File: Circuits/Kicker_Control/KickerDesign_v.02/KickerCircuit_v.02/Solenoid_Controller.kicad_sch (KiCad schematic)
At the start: 7 parts, among them Q2 NMOS, U4 VS-5EWH06FN-M3

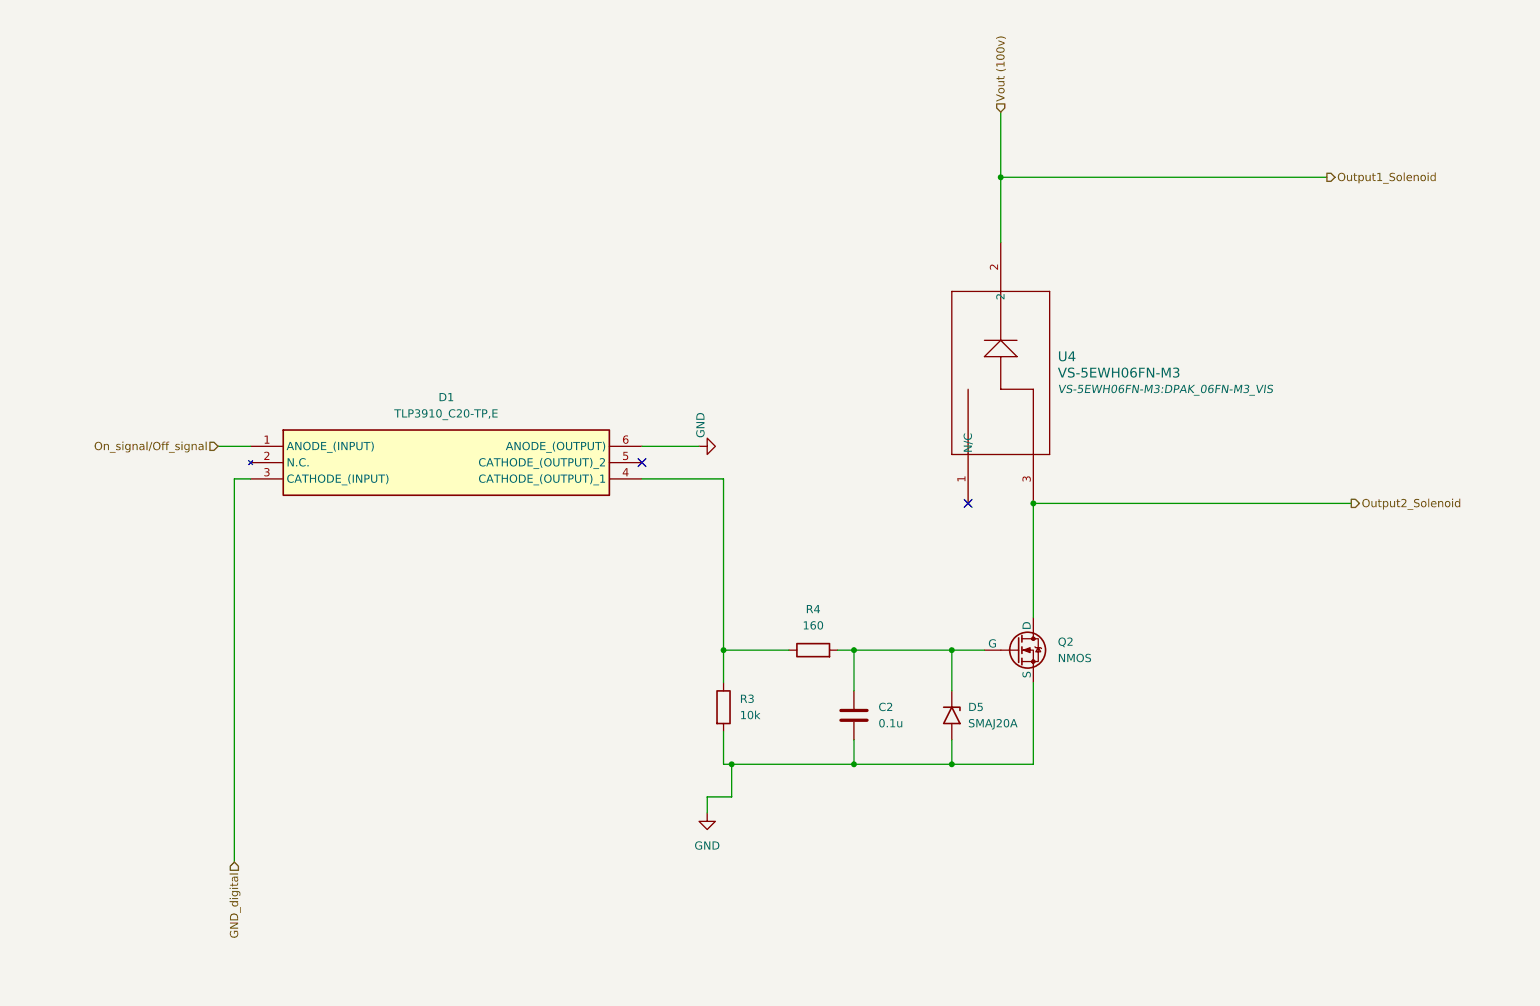
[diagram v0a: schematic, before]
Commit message: Changes in the kicker circuit
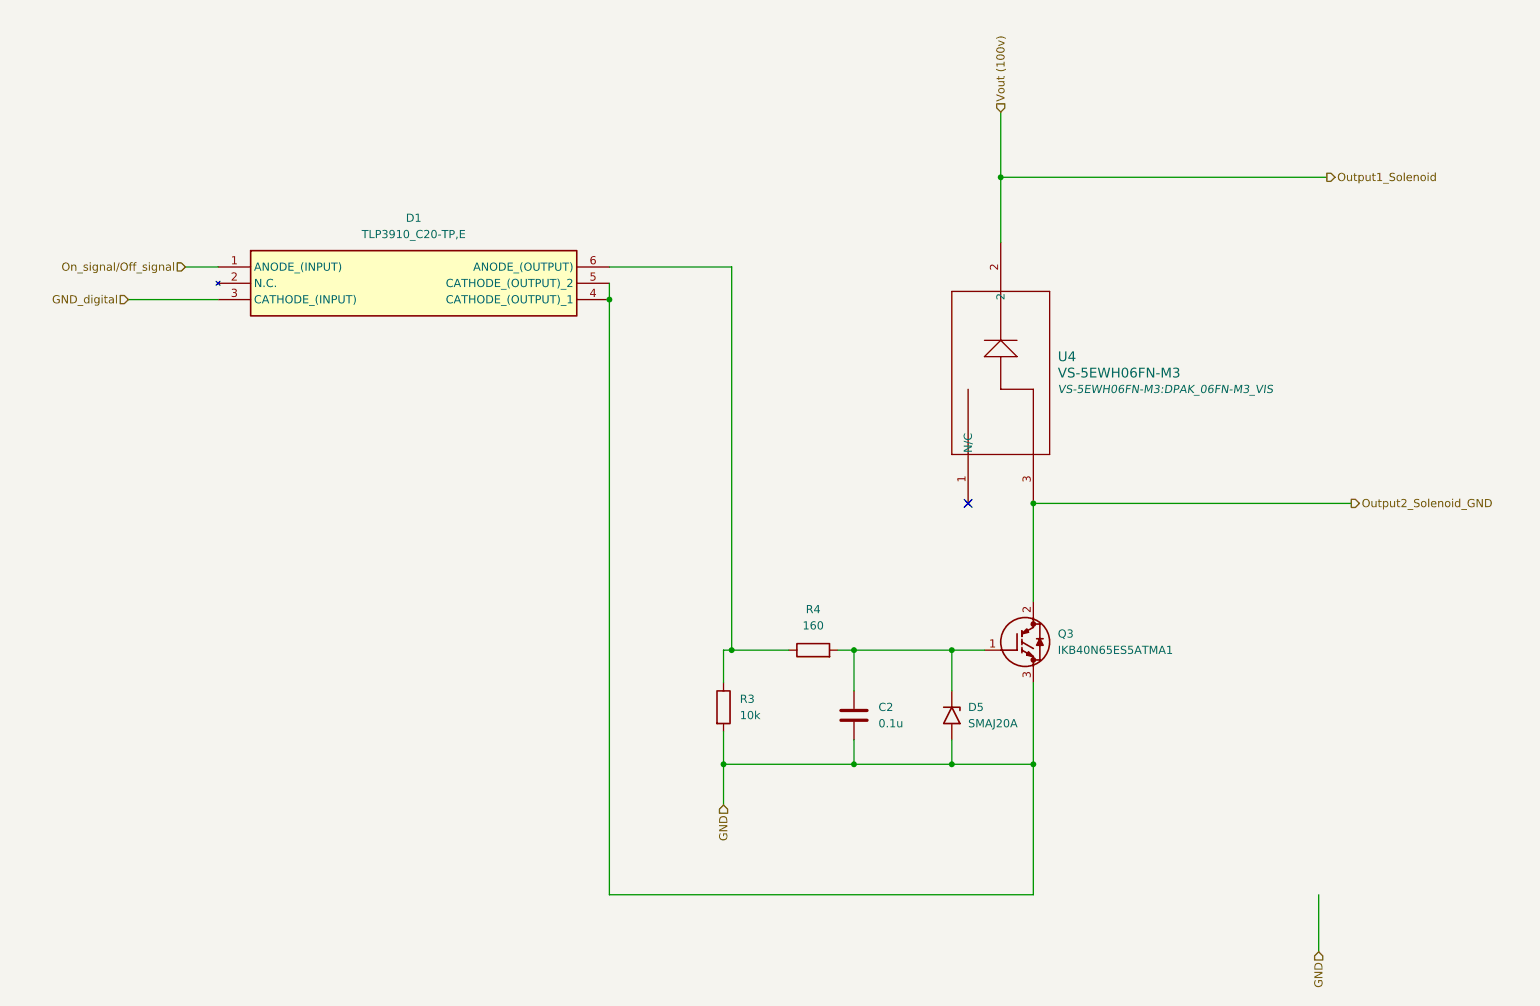
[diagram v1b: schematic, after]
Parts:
- removed Q2: NMOS, symbol Simulation_SPICE:NMOS
- added Q3: IKB40N65ES5ATMA1, BTS141TCBUMA1, symbol IKB40N65ES5ATMA1:IKB40N65ES5ATMA1
- D1: footprint SOIC127P1000X220-6N -> TLP3910_C20-TP,E:SOIC127P1000X220-6N
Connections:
- net GND: now also D1.4 (CATHODE_(OUTPUT)_1), D1.5 (CATHODE_(OUTPUT)_2), Q3.3 (E); no longer D1.6 (ANODE_(OUTPUT))
- net at C2.1, D5.1 (A1), R4.2: now also Q3.1 (G)
- net at R3.1, R4.1: now also D1.6 (ANODE_(OUTPUT)); no longer D1.4 (CATHODE_(OUTPUT)_1)
- net Output2_Solenoid renamed Output2_Solenoid_GND
- net Output2_Solenoid_GND: now also Q3.2 (C)
- no-connect marks 2 -> 1
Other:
- moved on the sheet: D1
